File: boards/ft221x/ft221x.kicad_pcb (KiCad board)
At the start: 2 copper layers, 17.8 x 26.7 mm, 11 parts, among them J1 USB_B_Micro, J2 BREADBOARD_A, J3 BREADBOARD_B, J4 BREAKOUT_SPI1, U1 FT221XS

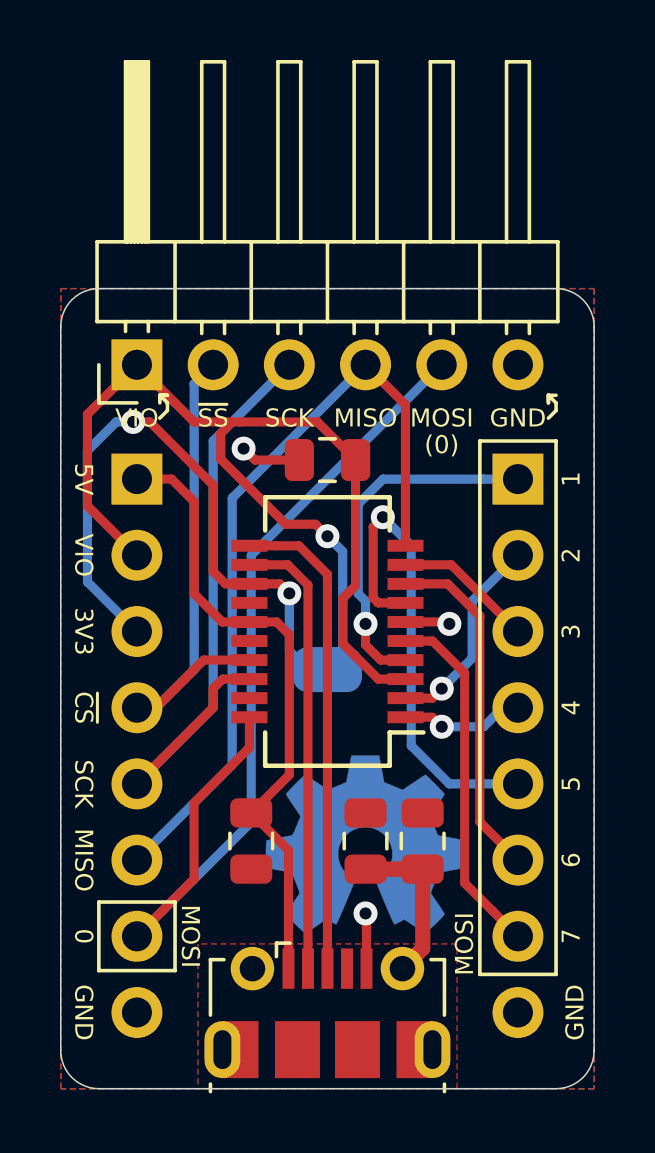
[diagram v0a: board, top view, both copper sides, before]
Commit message: Reduced board width. Reduced size of passives as a result.
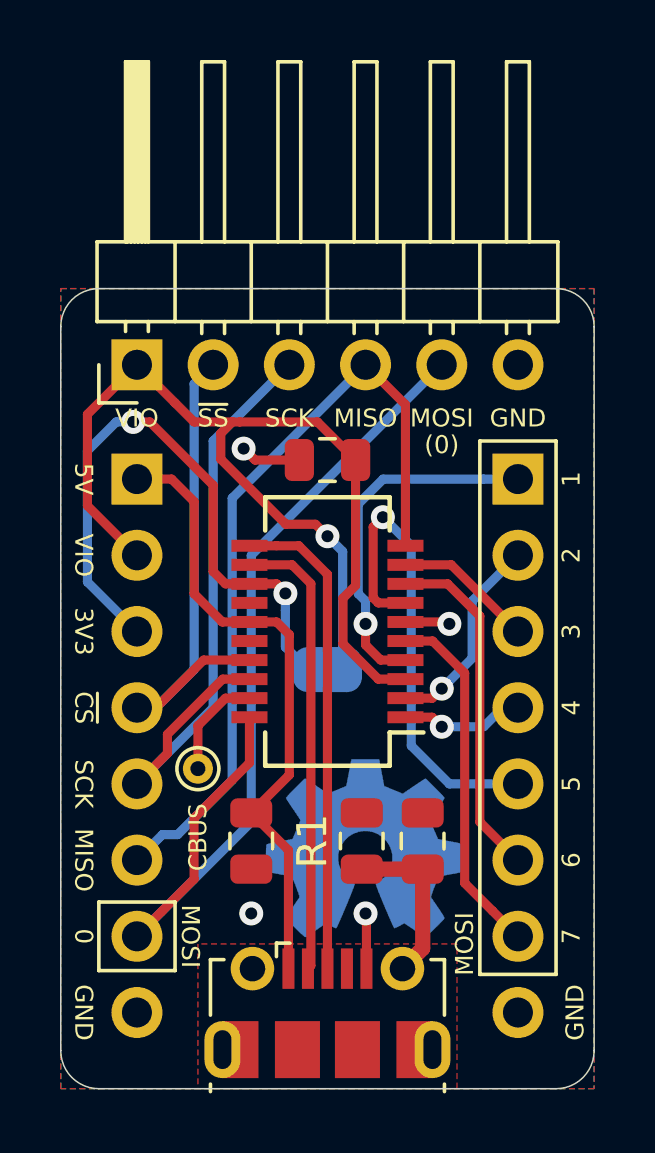
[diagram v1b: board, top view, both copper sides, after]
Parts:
- added CBUS: CBUS, TestPoint:TestPoint_THTPad_D1.0mm_Drill0.5mm, F.Cu at (24.9, 41.4)
- C1: value 100p -> 10n
- moved REF** 0.13 mm to (30.5, 44.1)
- moved R1 0.13 mm to (30.4, 43.8), turned to 90 degrees
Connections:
- R1 pad 1: GND -> Net-(C1-Pad2)
- R1 pad 2: Net-(C1-Pad2) -> GND
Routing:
- net /CBUS: track 0.00 -> 3.53 mm
- net GND: vias 3 -> 4
